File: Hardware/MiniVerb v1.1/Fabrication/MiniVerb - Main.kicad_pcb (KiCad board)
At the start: 2 copper layers, 85 x 128.5 mm, 59 parts, among them J1 IDC_2x05, U1 TL074, U2 TL074

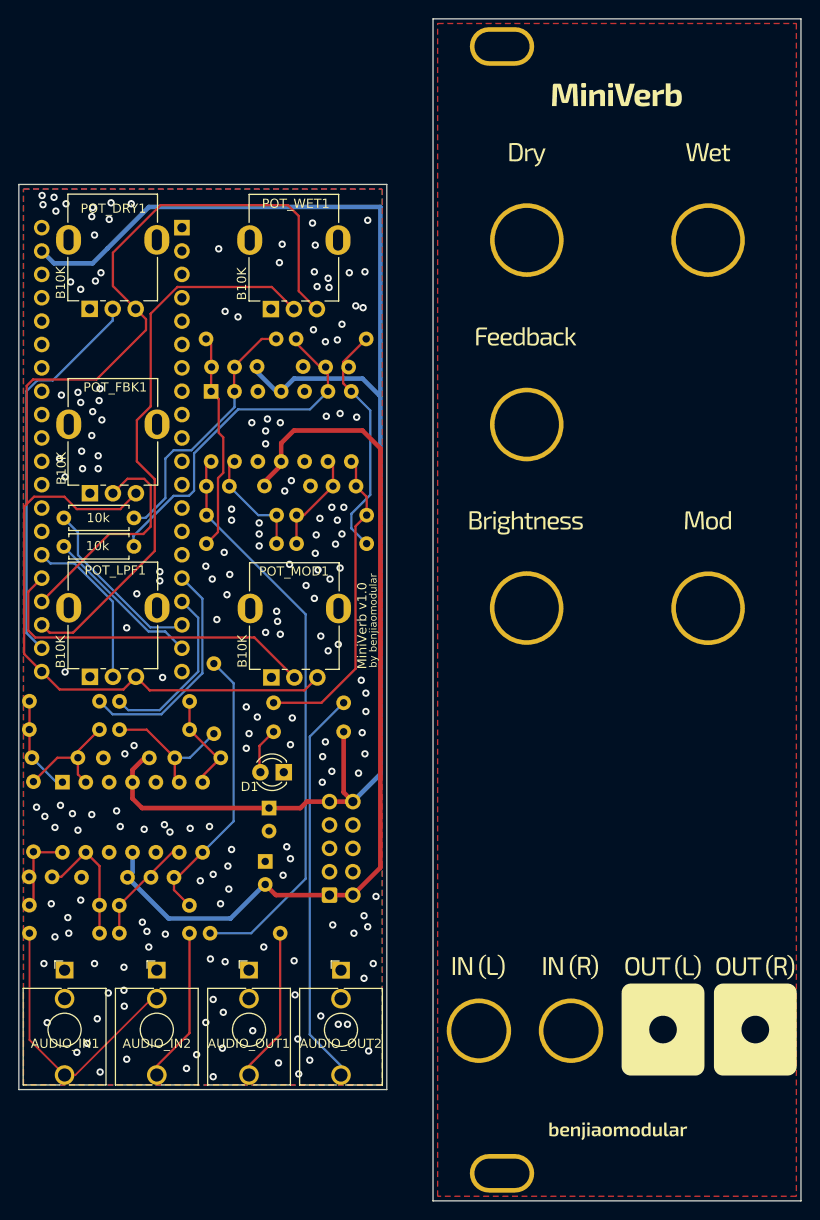
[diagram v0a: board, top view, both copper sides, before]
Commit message: Added SMT version
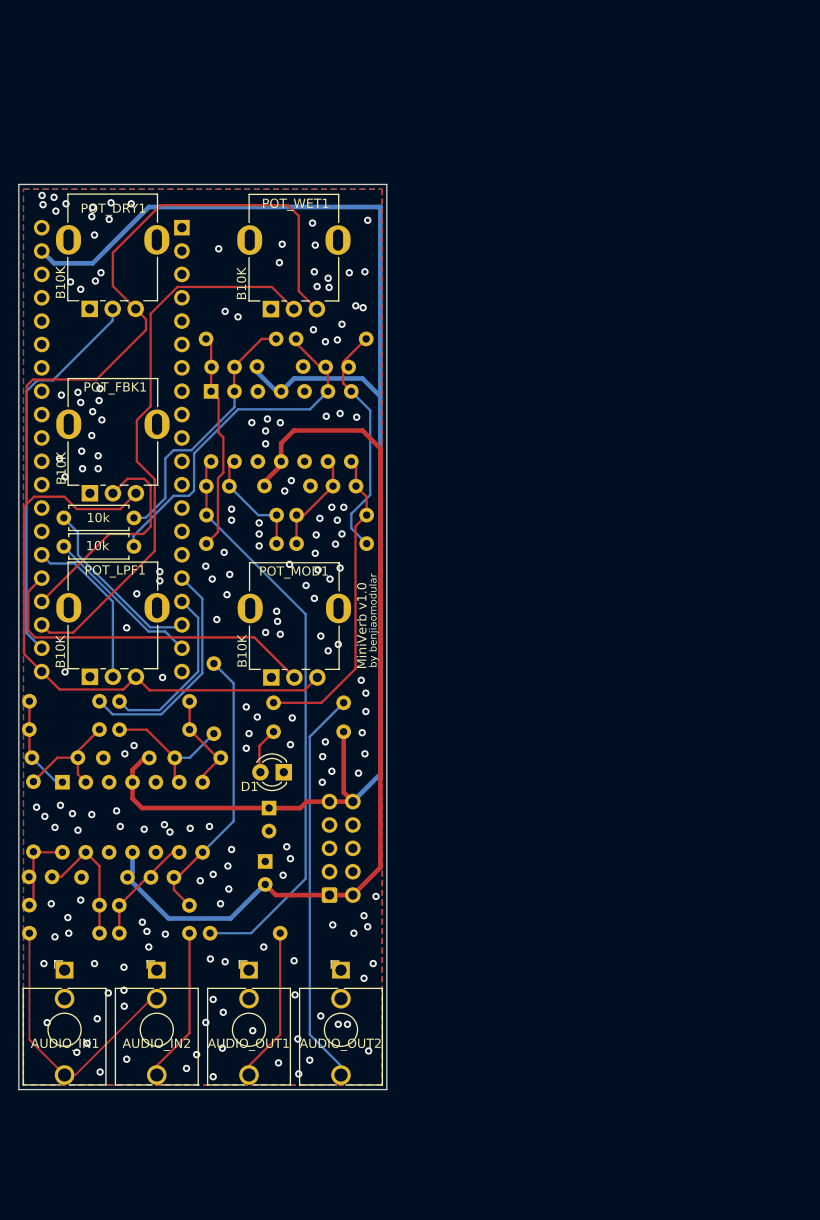
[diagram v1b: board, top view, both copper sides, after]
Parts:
- removed REF**: Panel_8HP, benjiaomodular:Panel_8HP
- removed REF** (x4): PanelHole_AudioJack_3.5mm, benjiaomodular:PanelHole_AudioJack_3.5mm
- removed REF** (x5): PanelHole_Potentiometer_RV09, benjiaomodular:PanelHole_Potentiometer_RV09
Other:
- board size 85 x 128.5 mm -> 40 x 98.4 mm
